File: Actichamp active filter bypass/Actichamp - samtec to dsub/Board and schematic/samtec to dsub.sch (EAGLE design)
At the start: 2 parts

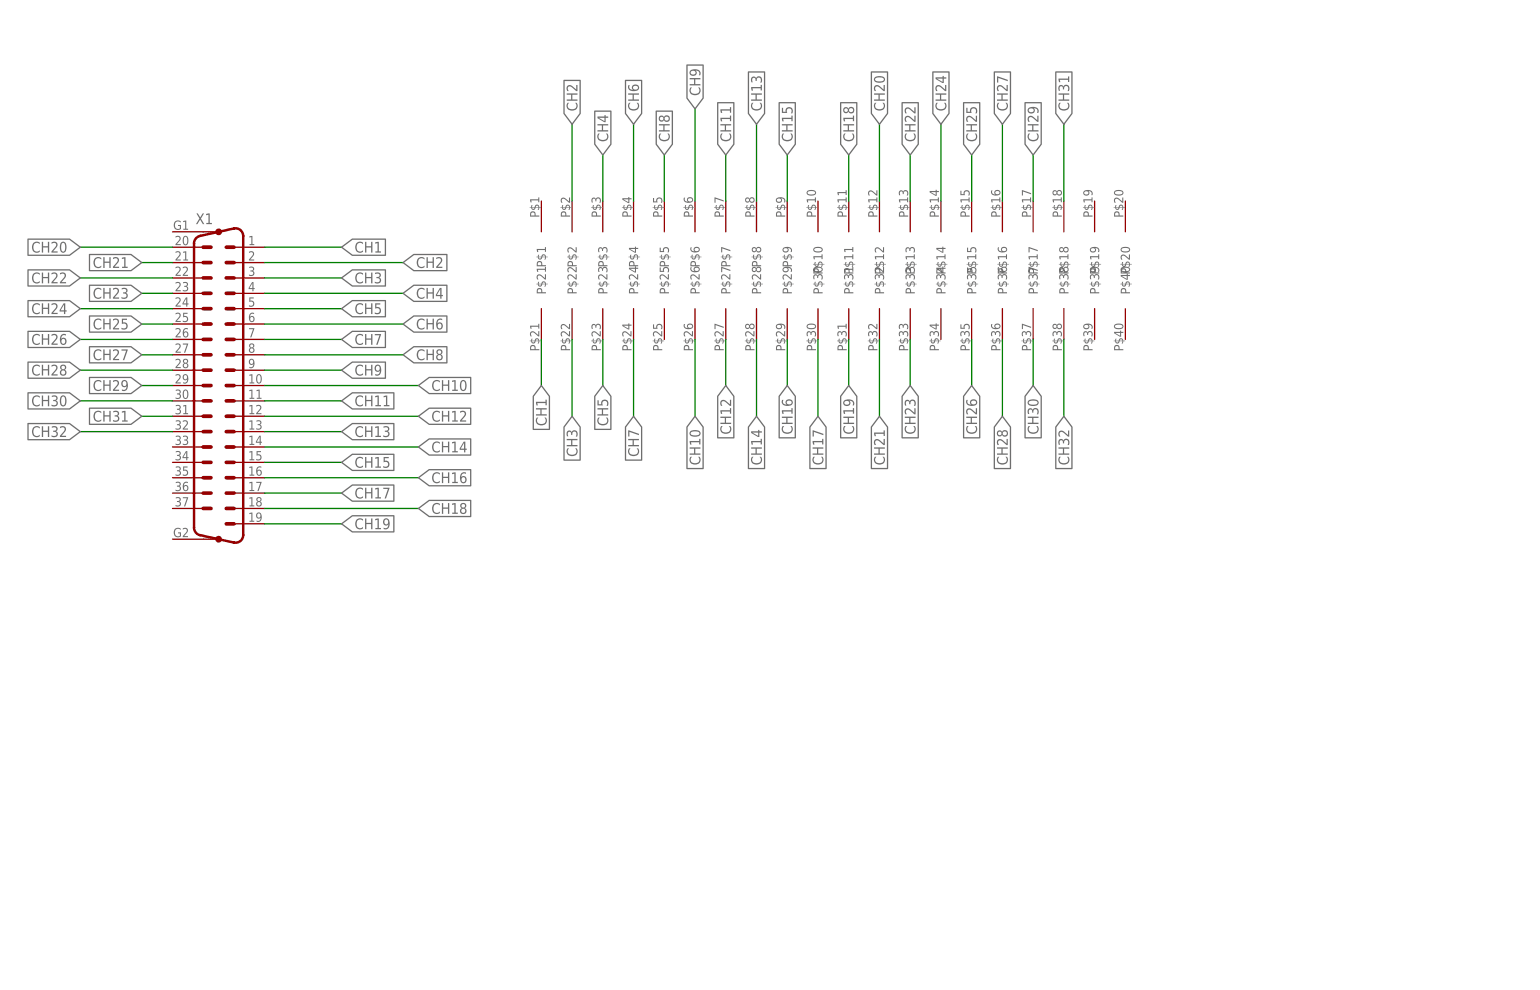
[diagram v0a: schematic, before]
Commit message: updated Dsub to Actichamp connector board. PCBWAY gerbers
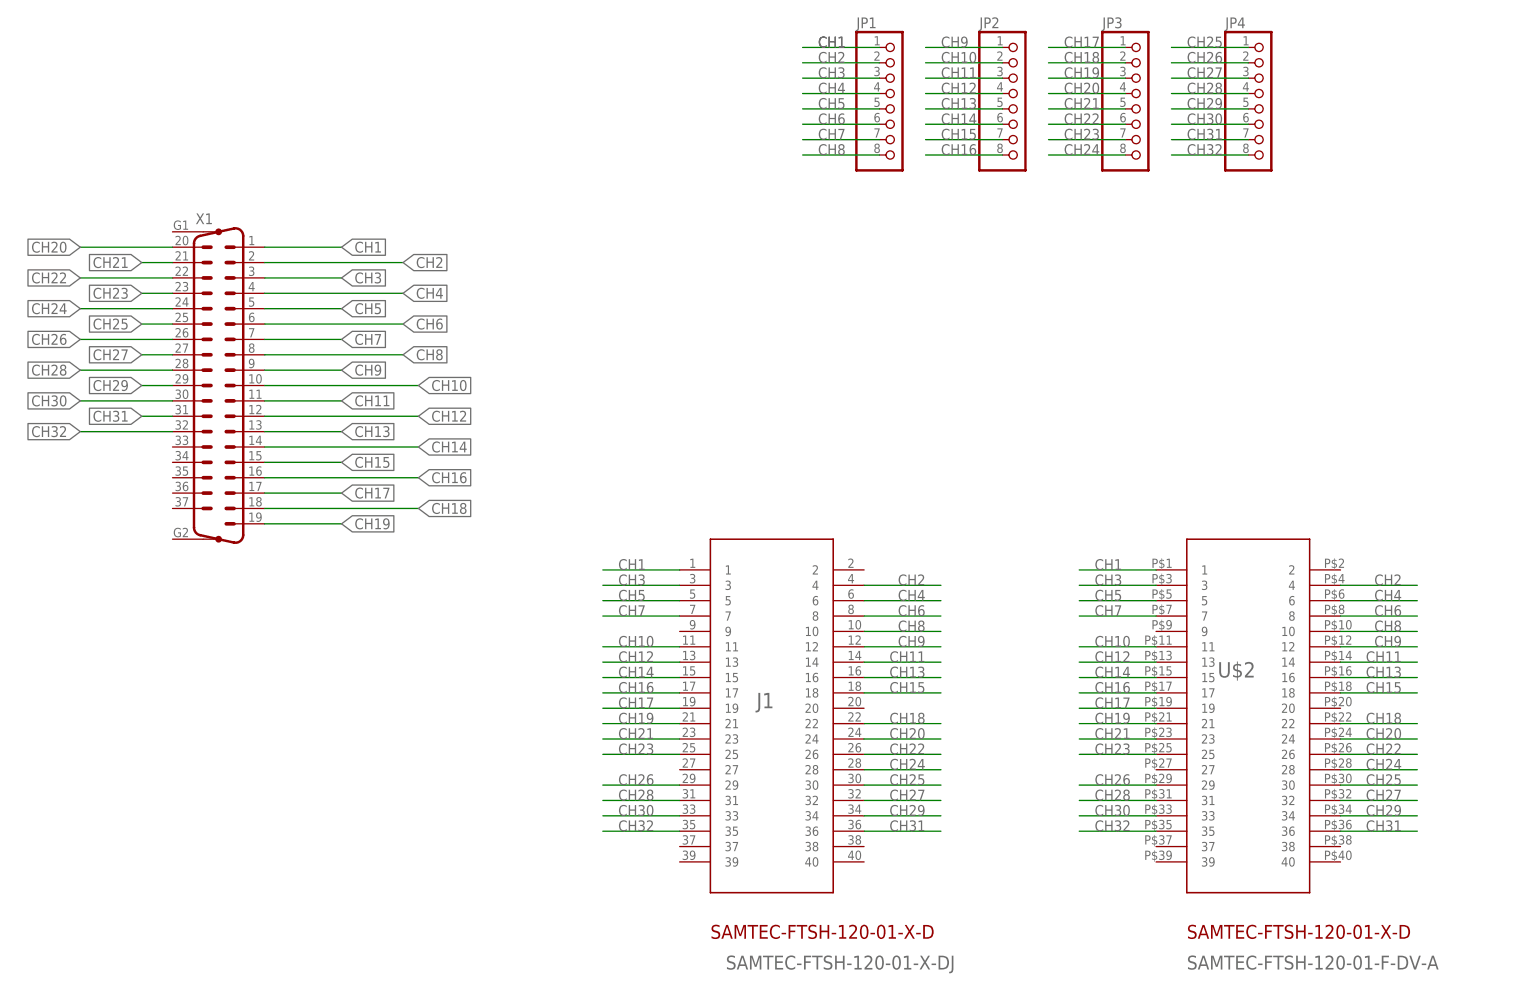
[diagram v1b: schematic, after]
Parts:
- removed U$1: SAMTEC_FTSH_LARGEPAD, mayo:SAMTEC_FTSH_LARGEPAD
- added J1: SAMTEC-FTSH-120-01-X-DJ, SAMTEC-FTSH-120-01-X-D:SAMTEC-FTSH-120-01-X-DJ
- added JP1, JP2, JP3, JP4: (no value), pinhead:PINHD-1X8
- added U$2: SAMTEC-FTSH-120-01-F-DV-A, samtec to dsub:SAMTEC-FTSH-120-01-F-DV-A
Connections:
- net CH1: now also J1.1, JP1.1, U$2.1; no longer U$1.P$21
- net CH10: now also J1.11, JP2.2, U$2.11; no longer U$1.P$26
- net CH11: now also J1.14, JP2.3, U$2.14; no longer U$1.P$7
- net CH12: now also J1.13, JP2.4, U$2.13; no longer U$1.P$27
- net CH13: now also J1.16, JP2.5, U$2.16; no longer U$1.P$8
- net CH14: now also J1.15, JP2.6, U$2.15; no longer U$1.P$28
- net CH15: now also J1.18, JP2.7, U$2.18; no longer U$1.P$9
- net CH16: now also J1.17, JP2.8, U$2.17; no longer U$1.P$29
- net CH17: now also J1.19, JP3.1, U$2.19; no longer U$1.P$30
- net CH18: now also J1.22, JP3.2, U$2.22; no longer U$1.P$11
- net CH19: now also J1.21, JP3.3, U$2.21; no longer U$1.P$31
- net CH2: now also J1.4, JP1.2, U$2.4; no longer U$1.P$2
- net CH20: now also J1.24, JP3.4, U$2.24; no longer U$1.P$12
- net CH21: now also J1.23, JP3.5, U$2.23; no longer U$1.P$32
- net CH22: now also J1.26, JP3.6, U$2.26; no longer U$1.P$13
- net CH23: now also J1.25, JP3.7, U$2.25; no longer U$1.P$33
- net CH24: now also J1.28, JP3.8, U$2.28; no longer U$1.P$14
- net CH25: now also J1.30, JP4.1, U$2.30; no longer U$1.P$15
- net CH26: now also J1.29, JP4.2, U$2.29; no longer U$1.P$35
- net CH27: now also J1.32, JP4.3, U$2.32; no longer U$1.P$16
- net CH28: now also J1.31, JP4.4, U$2.31; no longer U$1.P$36
- net CH29: now also J1.34, JP4.5, U$2.34; no longer U$1.P$17
- net CH3: now also J1.3, JP1.3, U$2.3; no longer U$1.P$22
- net CH30: now also J1.33, JP4.6, U$2.33; no longer U$1.P$37
- net CH31: now also J1.36, JP4.7, U$2.36; no longer U$1.P$18
- net CH32: now also J1.35, JP4.8, U$2.35; no longer U$1.P$38
- net CH4: now also J1.6, JP1.4, U$2.6; no longer U$1.P$3
- net CH5: now also J1.5, JP1.5, U$2.5; no longer U$1.P$23
- net CH6: now also J1.8, JP1.6, U$2.8; no longer U$1.P$4
- net CH7: now also J1.7, JP1.7, U$2.7; no longer U$1.P$24
- net CH8: now also J1.10, JP1.8, U$2.10; no longer U$1.P$5
- net CH9: now also J1.12, JP2.1, U$2.12; no longer U$1.P$6
